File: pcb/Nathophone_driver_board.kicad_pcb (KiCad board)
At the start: 4 copper layers, 160 x 110 mm, 223 parts, among them J1 PJ-063AH, J10 TERM BLOCK, J11 54202-S0806ALF, J12 54202-S0806ALF, J13 54202-S0806ALF, J14 54202-S0806ALF, J3 Conn_01x30, J4 54202-S0806ALF, J5 TERM BLOCK, J6 TERM BLOCK, J7 TERM BLOCK, J8 TERM BLOCK, J9 TERM BLOCK, Q1 2N7002H, Q10 BSS84, Q11 BSS84, Q12 2N7002H, Q13 2N7002H, Q2 2N7002H, Q3 FDN340P, Q4 FQD11P06TM, Q5 FDN340P, Q6 BSS84, Q7 BSS84, Q8 BSS84, Q9 BSS84, SW1 1-1571986-1, SW2 PTS645SM43SMTR92 LFS, SW3 DS04-254-2-01BK-SMT, U1 LT8650SEV_PBF, U10 74LVC2G07, U2 SPX3819M5-L-3-3, U3 TAS5720MRSMR, U4 TAS5720MRSMR, U5 TAS5720MRSMR, U6 TAS5720MRSMR, U7 TAS5720MRSMR, U8 TAS5720MRSMR

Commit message: FINISHED Version 1, Checked heights
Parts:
- added F1: Polyfuse, Fuse:Fuse_1812_4532Metric, F.Cu at (128.8, 124.5)
- added F2: Polyfuse, Fuse:Fuse_1812_4532Metric, F.Cu at (149.1, 135.4)
- added F3: Polyfuse, Fuse:Fuse_1206_3216Metric, F.Cu at (119.4, 124.5)
- added F4: Polyfuse, Fuse:Fuse_1206_3216Metric, F.Cu at (114.6, 124.5)
- added F5: Polyfuse, Fuse:Fuse_1206_3216Metric, F.Cu at (203.3, 132.3)
- added F6: Polyfuse, Fuse:Fuse_1206_3216Metric, F.Cu at (203.3, 134.6)
- added F7: Polyfuse, Fuse:Fuse_1206_3216Metric, F.Cu at (203.3, 130.0)
- moved D3 0.59 mm to (148.9, 141.8)
- moved R43 0.59 mm to (150.8, 138.5)
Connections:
- D12 pad 2: +5.3V -> Net-(D12-A)
- J11 pad 2: +3.3V_ext -> Net-(J11-Pin_2)
- J11 pad 4: +5V_ext -> Net-(J11-Pin_4)
- J12 pad 2: +24V -> Net-(J12-Pin_2)
- J12 pad 4: +5.3V -> Net-(J12-Pin_4)
- J12 pad 6: +3.3V_int -> Net-(J12-Pin_6)
- J4 pad 5: +3.3V_int -> Net-(J4-Pin_5)
- J4 pad 7: +3.3V_int -> Net-(J4-Pin_5)
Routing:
- net +5.3V: track 214.5 -> 200.7 mm
- net Net-(J11-Pin_2): track 0.00 -> 12.3 mm
- net Net-(J11-Pin_4): track 0.00 -> 12.0 mm
- net +3.3V_ext: track 120.7 -> 132.3 mm
- net +5V_ext: track 36.3 -> 47.7 mm
- net Net-(J12-Pin_6): track 0.00 -> 10.1 mm
- net Net-(J4-Pin_5): track 0.00 -> 9.65 mm
- net Net-(J12-Pin_4): track 0.00 -> 9.61 mm
- net Net-(J12-Pin_2): track 0.00 -> 9.50 mm
- net +24V: track 104.8 -> 96.0 mm
- net Net-(D12-A): track 0.00 -> 7.48 mm
- net +3.3V_int: track 133.0 -> 128.2 mm
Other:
- board text added: "+ -"
- board text added: "+24V"
- board text added: "+3.3V_ext"
- board text added: "+3.3V_int"
- board text added: "+5.3V"
- board text added: "+5V_ext"
- board text added: "1-2 = Burst Open = FCM 2-3 = SSM"
- board text added: "24V IN 90W"
- board text added: "DATA"
- board text added: "Ext. Reset"
- board text added: "GND"
- board text added: "GPIO"
- board text added: "LRCLK"
- board text added: "MRCLK"
- board text added: "Man. Reset"
- board text added: "NC"
- board text added: "Nathophone Driver Board v1 by Nathanael Gubler, Okt. 2025 Juventus Technikerschule HF"
- board text added: "OFF"
- board text added: "ON"
- board text added: "OUT1 -/+"
- board text added: "OUT2 -/+"
- board text added: "OUT3 -/+"
- board text added: "OUT4 -/+"
- board text added: "OUT5 -/+"
- board text added: "OUT6 -/+"
- board text added: "PG_1"
- board text added: "PG_2"
- board text added: "SCL"
- board text added: "SCLK"
- board text added: "SDA"
- board text added: "System Connector"
- board text added: "U1_temp"
- board text added: "~{ADC_RST_N_OUT}"
- board text added: "~{FAULT_0}"
- board text added: "~{FAULT_1}"
- board text added: "~{FAULT_2}"
- board text added: "~{FAULT_3}"
- board text added: "~{FAULT_4}"
- board text added: "~{FAULT_5}"
- board text added: "~{Group SDZ}"

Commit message: CHANGED small things, removed tiny 0201 cap
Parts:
- C7: footprint Capacitor_SMD:C_0201_0603Metric_Pad0.64x0.40mm_HandSolder -> Capacitor_SMD:C_0402_1005Metric
- moved C7 0.21 mm to (206.7, 87.4)
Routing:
- net +15V: track 51.7 -> 50.8 mm
- net GND: vias 538 -> 546
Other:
- board text added: "Power ON"

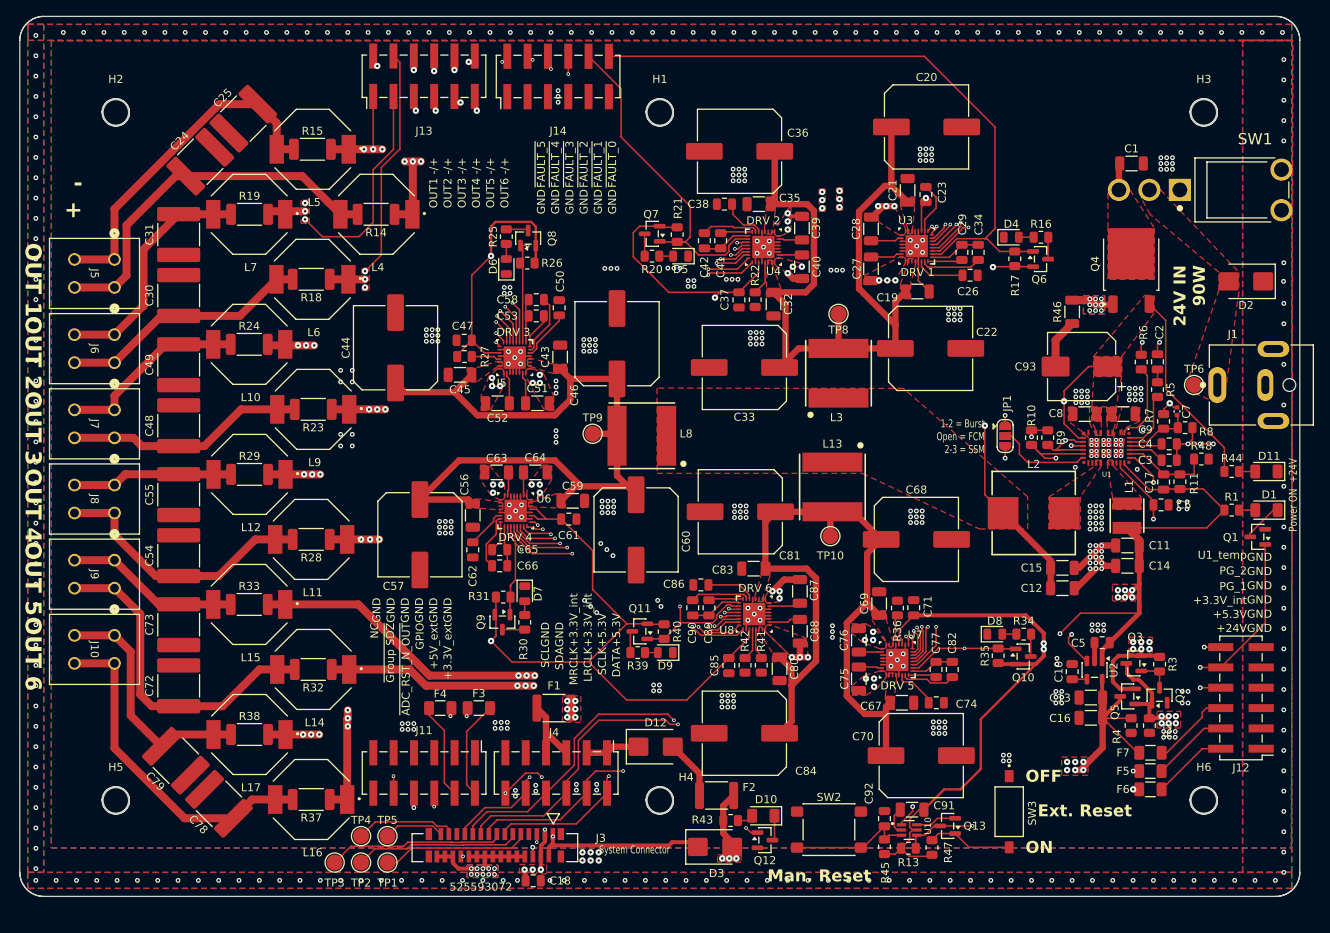
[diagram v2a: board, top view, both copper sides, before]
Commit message: CHANGED little tweaks in the Ground path, removed unnecessary Diode
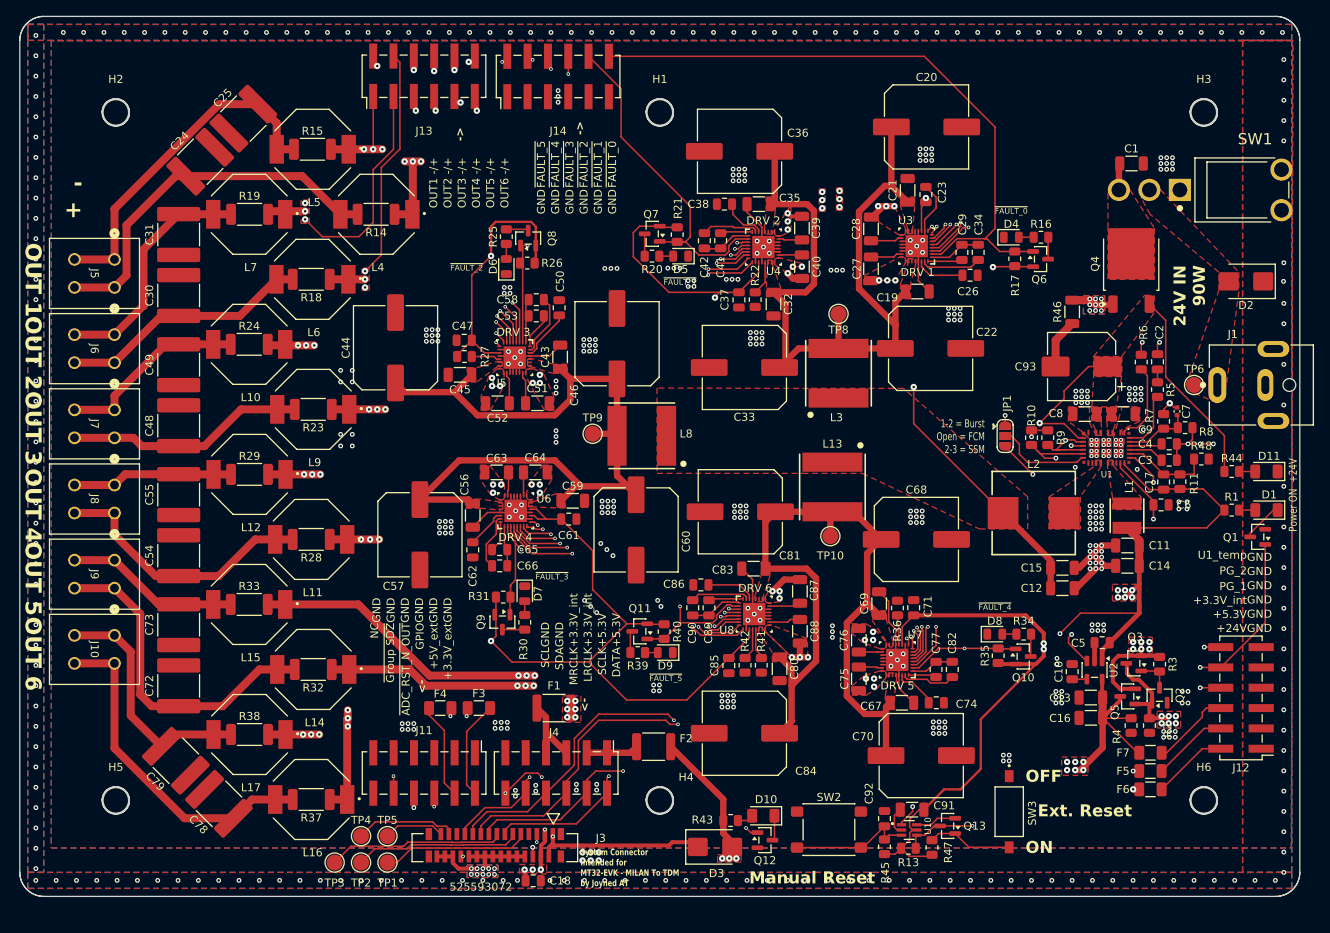
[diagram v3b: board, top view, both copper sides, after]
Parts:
- removed D12: SL215B-TP, Diode_SMD:D_SMB
- moved F2 9.96 mm to (141.2, 129.3)
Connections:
- F2 pad 2: Net-(D12-A) -> Net-(J4-Pin_1)
- J4 pad 1: Net-(D12-K) -> Net-(J4-Pin_1)
- J4 pad 3: Net-(D12-K) -> Net-(J4-Pin_1)
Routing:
- net GND: track 149.6 -> 178.4 mm
- net +15V: track 50.8 -> 68.7 mm
- net +5.3V: track 200.7 -> 209.0 mm
- net Net-(D12-A): track 7.48 -> 0.00 mm
- net Net-(D12-K): track 6.79 -> 0.00 mm
- net Net-(J4-Pin_1): track 0.00 -> 6.54 mm
- net VCC_REG: track 39.3 -> 38.4 mm
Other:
- board text added: "->"
- board text added: "Manual Reset"
- board text added: "System Connector Intended for MT32-EVK - MILAN To TDM by Joyned AT"
- board text removed: "Man. Reset"
- board text removed: "System Connector"
